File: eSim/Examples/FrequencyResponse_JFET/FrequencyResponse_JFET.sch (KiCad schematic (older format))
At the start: 12 parts, among them J1 NJF, U1 plot_v1, U2 plot_phase, U3 plot_log, U4 plot_db

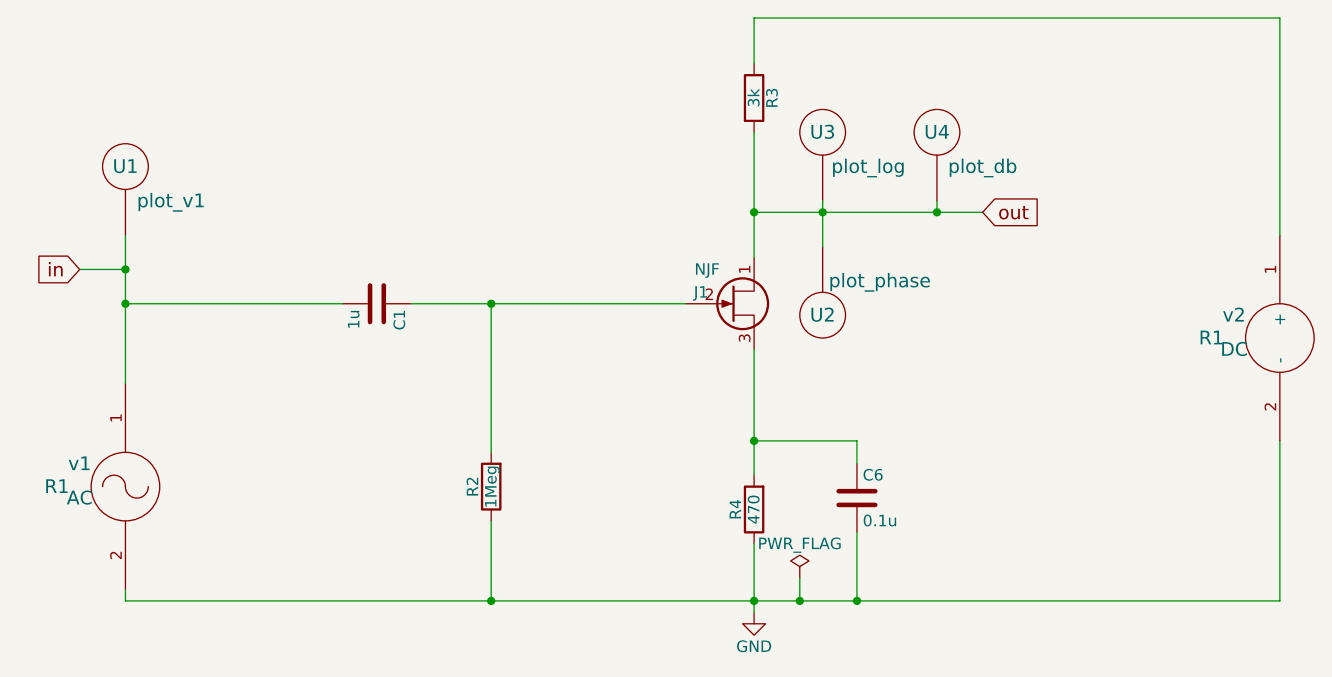
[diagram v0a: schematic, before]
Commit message: permission and online-offline mode
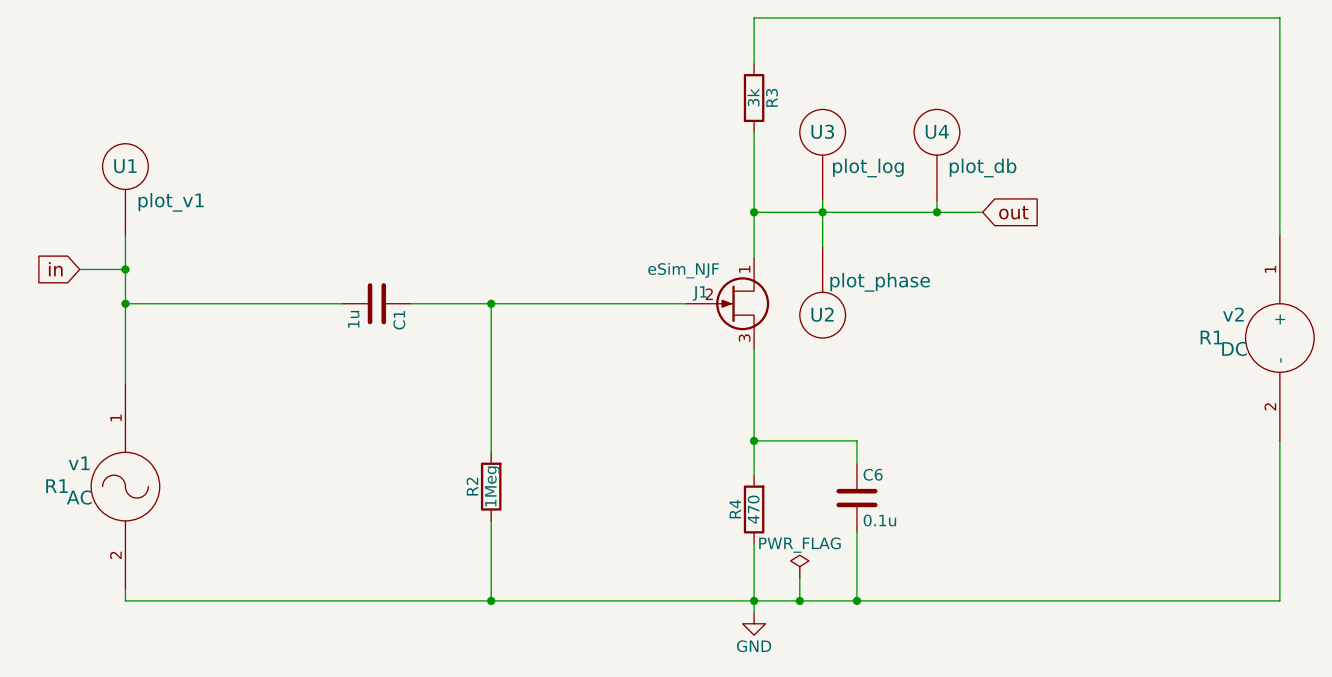
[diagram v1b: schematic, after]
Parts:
- removed J1: NJF, symbol NJF
- added J1: eSim_NJF, symbol eSim_NJF
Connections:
- net out: now also J1.1 (D)
- net at C1.1, R2.2: now also J1.2 (G)
- net at C6.1, R4.2: now also J1.3 (S)
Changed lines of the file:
@@
 Connection ~ 5150 4800
-$Comp
-L NJF J1
-U 1 1 557065CE
-P 6200 3500
-F 0 "J1" H 6100 3550 50  0000 R CNN
-F 1 "NJF" H 6150 3650 50  0000 R CNN
-F 2 "" H 6400 3600 29  0000 C CNN
-F 3 "" H 6200 3500 60  0000 C CNN
-	1    6200 3500
-	1    0    0    -1
-$EndComp
 $Comp
 L R-RESCUE-FrequencyResponse_JFET R3
@@
 	6500 4700 6500 4800
 Connection ~ 6500 4800
+$Comp
+L eSim_NJF J1
+U 1 1 5D676E10
+P 6200 3500
+F 0 "J1" H 6100 3550 50  0000 R CNN
+F 1 "eSim_NJF" H 6150 3650 50  0000 R CNN
+F 2 "" H 6400 3600 29  0000 C CNN
+F 3 "" H 6200 3500 60  0000 C CNN
+	1    6200 3500
+	1    0    0    -1
+$EndComp
 $EndSCHEMATC
